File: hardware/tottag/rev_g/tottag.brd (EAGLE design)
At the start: 68.1 x 39.6 mm, 203 parts, among them J1 USB4110-GF-A, J2 DM3AT-SF-PEJM5, J3 TC2030-JLINK-NL-2SIDE, J4 TC2030-JLINK-NL-2SIDE, J5 MOLEX-PICO-SPOX-3SIDE, Q1 CSD75207W15, Q4 CSD75207W15, T1 HHM1595A1, U1 DW1000, U10 STM32F091CC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

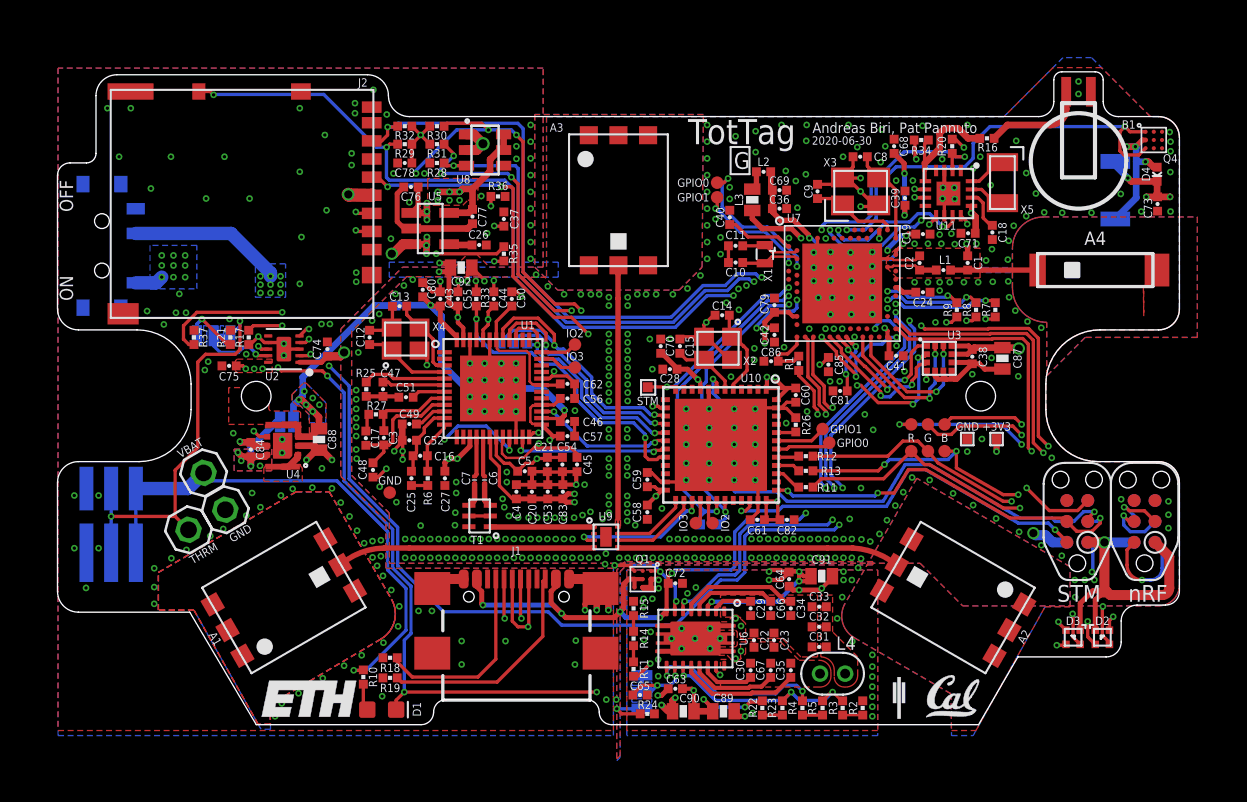
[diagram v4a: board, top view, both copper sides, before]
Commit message: rev_g: clean up planes
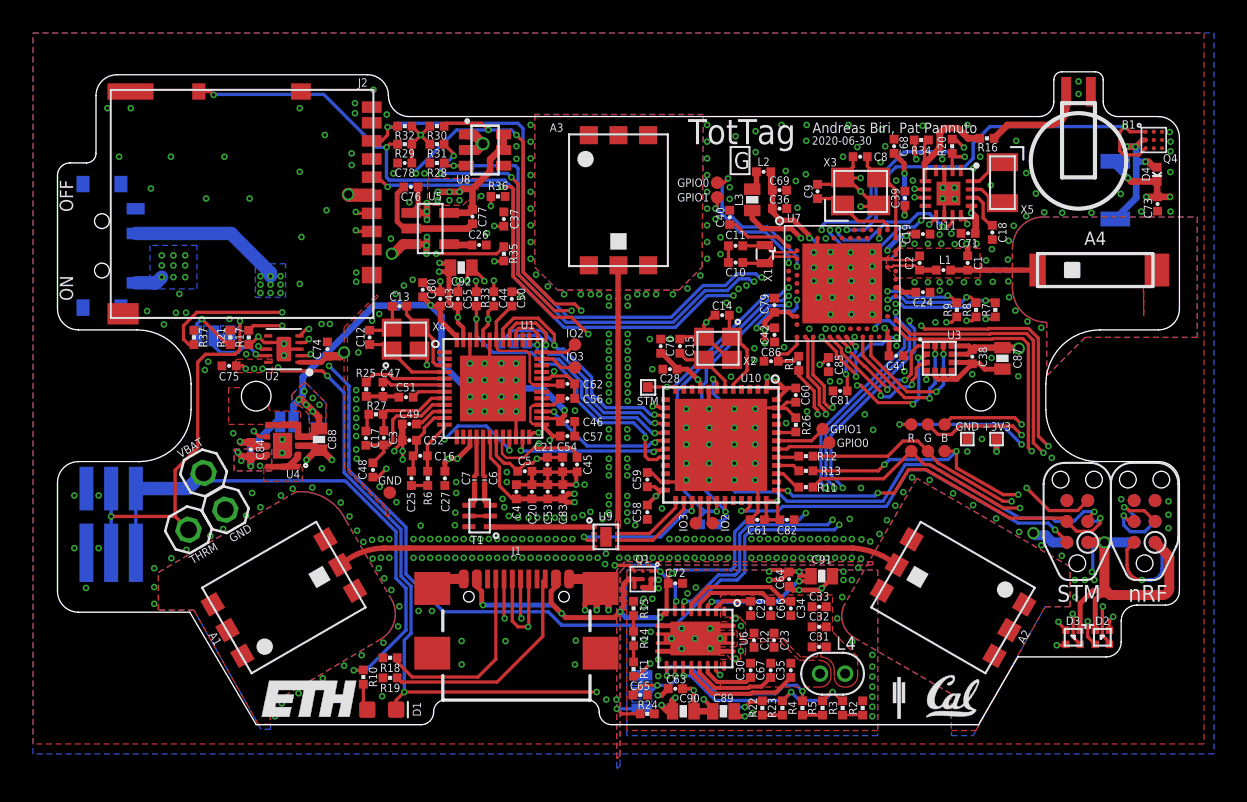
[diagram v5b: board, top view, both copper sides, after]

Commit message: rev_g: a bit more plane work
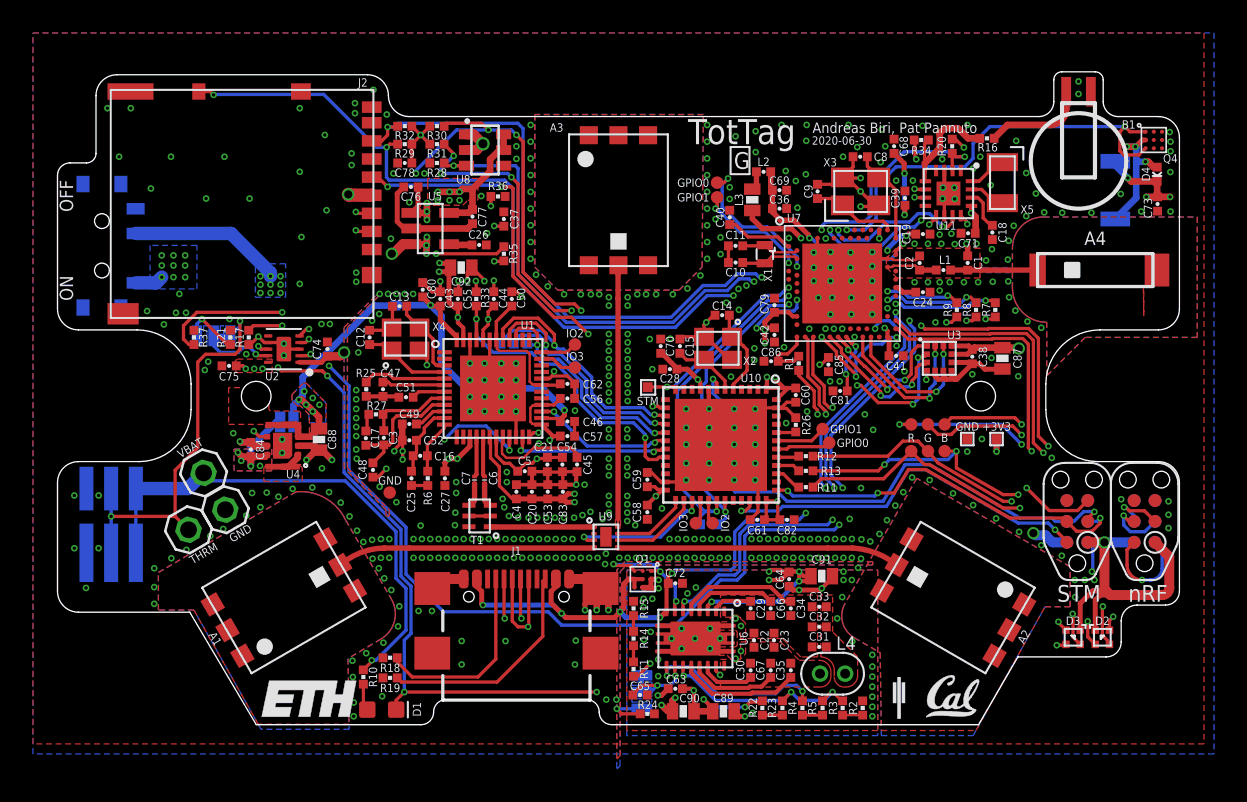
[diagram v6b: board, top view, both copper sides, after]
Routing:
- net VQI: track 17.6 -> 19.7 mm
- net VBAT: track 72.2 -> 71.0 mm
- net GND: vias 544 -> 546

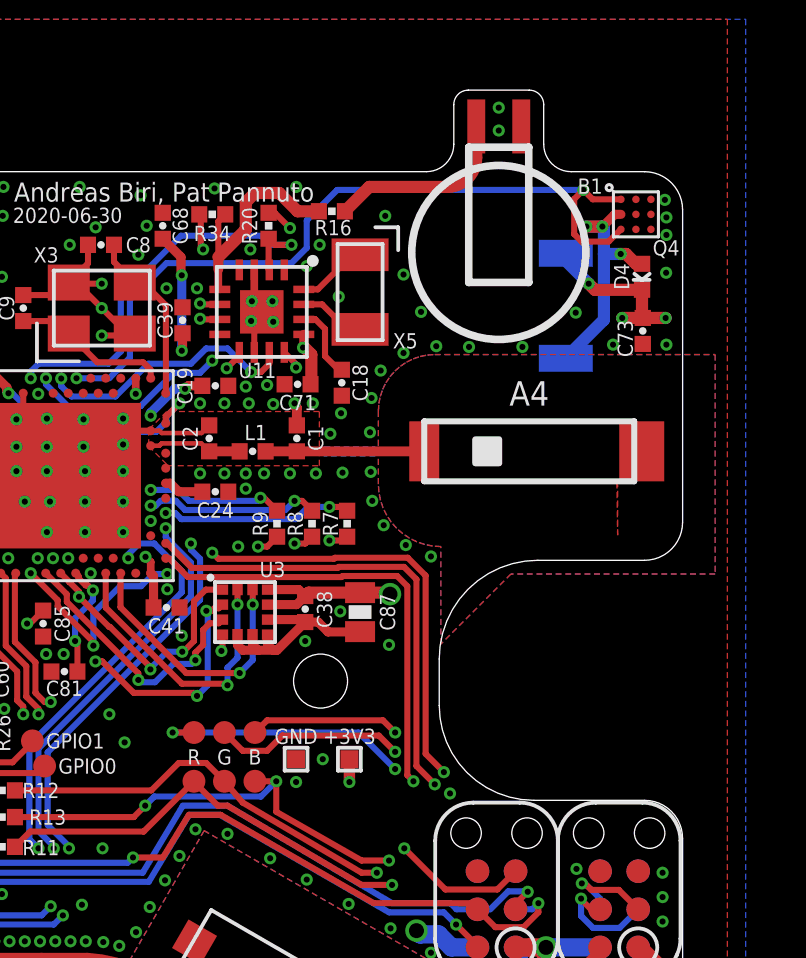
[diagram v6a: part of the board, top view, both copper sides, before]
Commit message: rev_g: update BLE antenna layout with new understanding
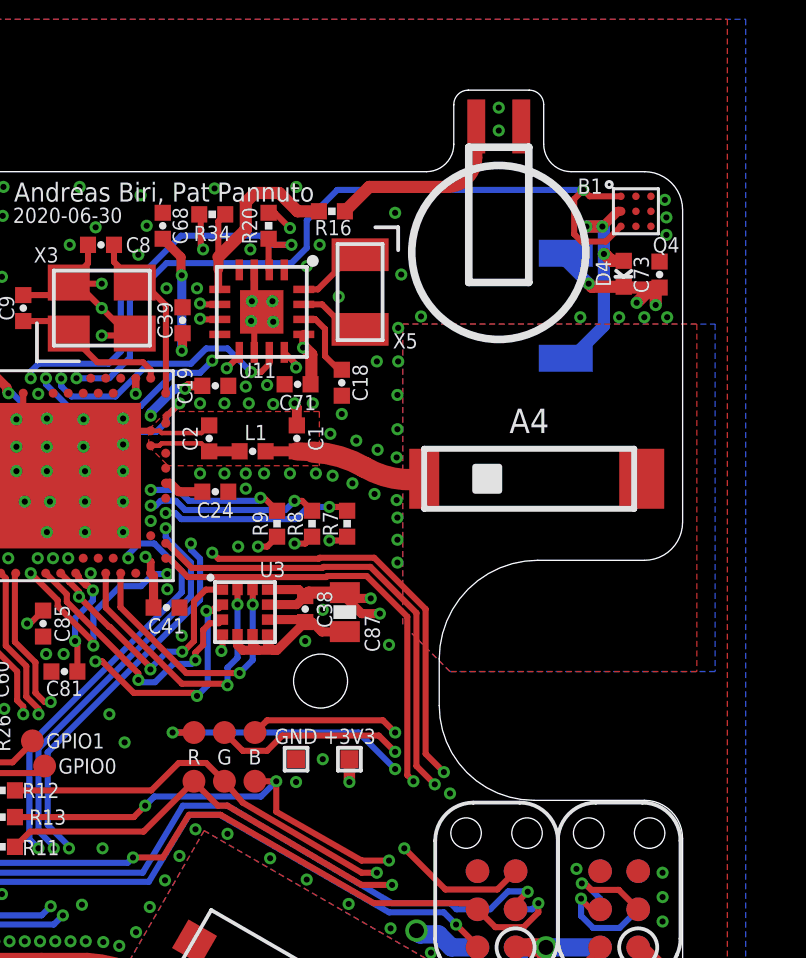
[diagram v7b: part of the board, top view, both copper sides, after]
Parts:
- moved C73 1.96 mm to (33.3, 27.1), turned to 90 degrees
- moved A4 0.91 mm to (29.0, 20.2)
- moved D4 0.62 mm to (32.1, 27.1)
- moved C87 0.51 mm to (22.8, 15.8)
- moved Q4 0.10 mm to (32.5, 29.2)
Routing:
- net +3V3: track 144.6 -> 145.3 mm, vias 41 -> 42
- net N$59: track 36.2 -> 35.5 mm
- net !NRF_RST: track 30.6 -> 29.9 mm
- net NRF_SWDCLK: track 27.0 -> 26.4 mm
- net N$60: track 36.2 -> 35.6 mm
- net N$61: track 34.7 -> 34.2 mm
- net NRF_SWDIO: track 33.1 -> 32.5 mm
- net GND: track 173.6 -> 173.0 mm, vias 546 -> 548
- added copper zone on layer 2, net N$17
- removed copper zone on layer 16, net N$17
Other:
- board text added: "Nordic forums suggest higher parasitics if waveguide is made with internal layers, so block copper on inner layers. Trace width calc's for coplanar wave: 28 mil Conductor W 59 mil (1.6 mm) Conductor H 4 mil Conductor Gap [must match DW traces for single plane pour] ~= 49.999 ohm"
- board text added: "https://abracon.com/uploads/resources/AMCA-Series-Multilayer-Chip-Antenna-Application-Note.pdf Goal is 10mm no-metal width, antenna in center (doc lines are 5mm) Goal is 14mm no-metal length, from plane edge (goes off board, no problem) Seems to be no feed gap in reference design RTC battery nearby is.. unfortunate"
- board text removed: "Metal spacing here is a guess. The datasheet simply says no ground.. so follow what worked well for the UWB ones"

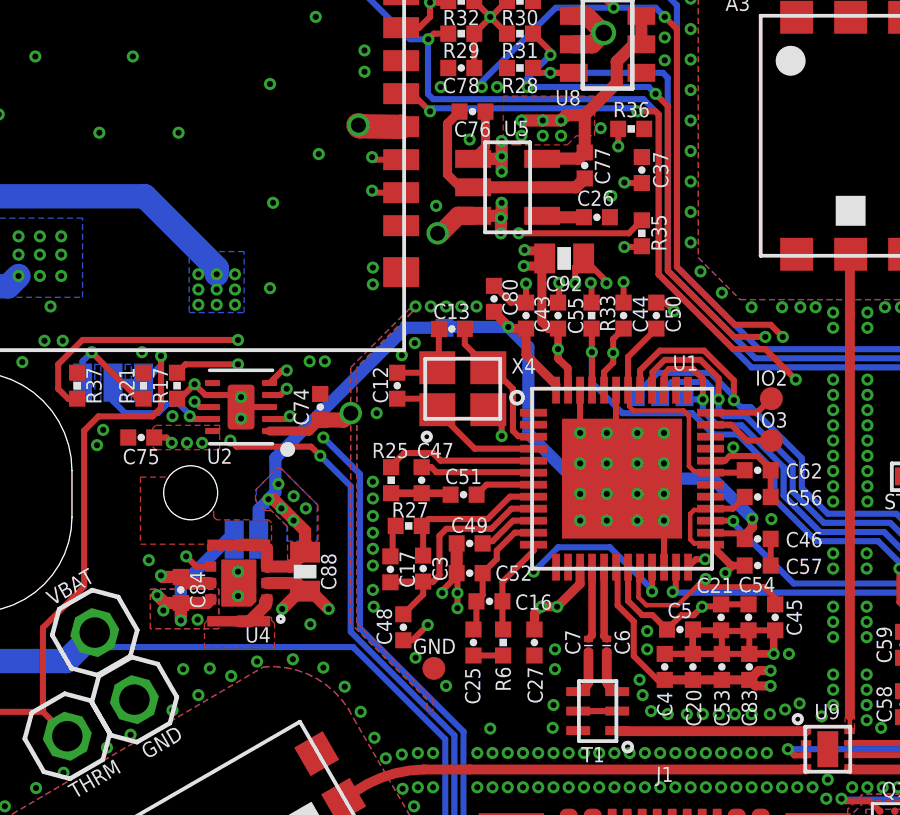
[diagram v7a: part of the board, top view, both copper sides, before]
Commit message: rev_g: improve U2 GND connections; fatten up +3v3 entry
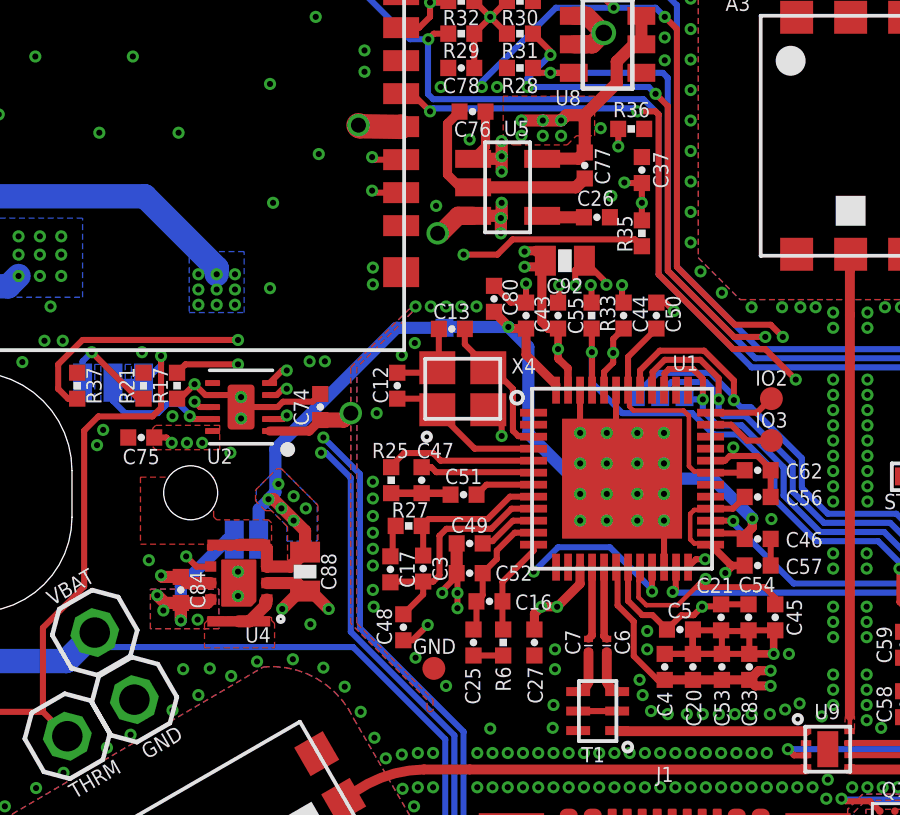
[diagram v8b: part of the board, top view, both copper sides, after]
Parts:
- moved C92 0.08 mm to (-9.53, 21.2)
- turned R35 to 270 degrees
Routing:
- net GND: track 173.0 -> 174.7 mm
